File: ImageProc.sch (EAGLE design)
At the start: 93 parts, among them IC1 XC61GC3002HR-G, IC2 MIC5335-SPYMT, IC5 AT86RF233-ZU, IC6 LTC6088, IC7 DRV8833RTY, IC8 DRV8833RTY, IC9 MPU-6000, J1 CON-HRS-DM3AT, P1 BAT+, P10 MD2, P2 BAT-, P3 MA1, P4 MA2, P5 MB1, P6 MB2, P7 MC1, P8 MC2, P9 MD1, U1 CY8C5688LTI-LP086

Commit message: Major board layout jumble. Lots of placeholder connections.
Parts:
- removed R12, R17, R22: 15k, biomimetic:RESISTOR0402-RES
- removed R16, R18: 4.7k, biomimetic:RESISTOR0402-RES
- added JP6: USBSMD, SparkFun-Connectors:USBSMD
- R8: device biomimetic:RESISTOR0402-RES -> OPL Eagle Library:R-4R; TOLERANCE 1% -> (none)
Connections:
- removed net !SS2_2: IC9S.!CS
- new net !SS2: IC9S.!CS, U1G$6./SS2_2
- new net EMFILE_CS: U1G$3.EMFILE_CS
- new net EMFILE_MISO: U1G$3.EMFILE_MISO
- new net EMFILE_MOSI: U1G$3.EMFILE_MOSI
- new net EMFILE_SCK: U1G$3.EMFILE_SCK
- new net USB_D+: JP6.D+, U1G$6.USB_D+
- new net USB_D-: JP6.D-, U1G$6.USB_D-
- net !SS1: now also U1G$6./SS1
- net 3.3V: now also J1.VDD; no longer R16.2
- net BATT_LEVEL: now also U1G$1.VBATT_SENSE
- net GND: now also J1.VSS; no longer R18.1
- net GN_LED: now also U1G$4.GREEN_LED
- net MOTOR_A_BEMF: now also U1G$1.BEMFA
- net MOTOR_A_IN1: now also U1G$5.PWMA_1
- net MOTOR_A_IN2: now also U1G$5.PWMA_2
- net MOTOR_B_BEMF: now also U1G$1.BEMFB
- net MOTOR_B_IN1: now also U1G$5.PWMB_1
- net MOTOR_B_IN2: now also U1G$5.PWMB_2
- net MOTOR_C_BEMF: now also U1G$1.BEMFC
- net MOTOR_C_IN1: now also U1G$5.PWMC_1
- net MOTOR_C_IN2: now also U1G$5.PWMC_2
- net MOTOR_D_BEMF: now also U1G$1.BEMFD
- net MOTOR_D_IN1: now also U1G$5.PWMD_1
- net MOTOR_D_IN2: now also U1G$5.PWMD_2
- net N$22: now also R8B.1; no longer R12.1
- net N$24: now also R8C.1; no longer R17.1
- net N$26: now also R8D.1; no longer R22.1
- net N$30: now also R8A.1; no longer R8.1
- net N$34: now also R8D.2; no longer R22.2
- net N$35: now also R8C.2; no longer R17.2
- net N$36: now also R8A.2; no longer R8.2
- net N$37: now also R8B.2; no longer R12.2
- net RD_LED: now also U1G$4.RED_LED
- net SCK1: now also U1G$6.SCK1
- net SCK2: now also U1G$6.SCK2
- net SCL1: now also U1G$6.SCL1
- net SDA1: now also U1G$6.SDA1
- net SDI1: now also U1G$6.MISO1
- net SDI2: now also U1G$6.MISO2
- net SDO1: now also U1G$6.MOSI1
- net SDO2: now also U1G$6.MOSI2
- net V_REF: no longer R16.1, R18.2
- net YW_LED: now also U1G$4.YELLOW_LED
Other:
- moved on the sheet: C26, R4, R5, U1G$1, U1G$2, U1G$3, U1G$4, U1G$6

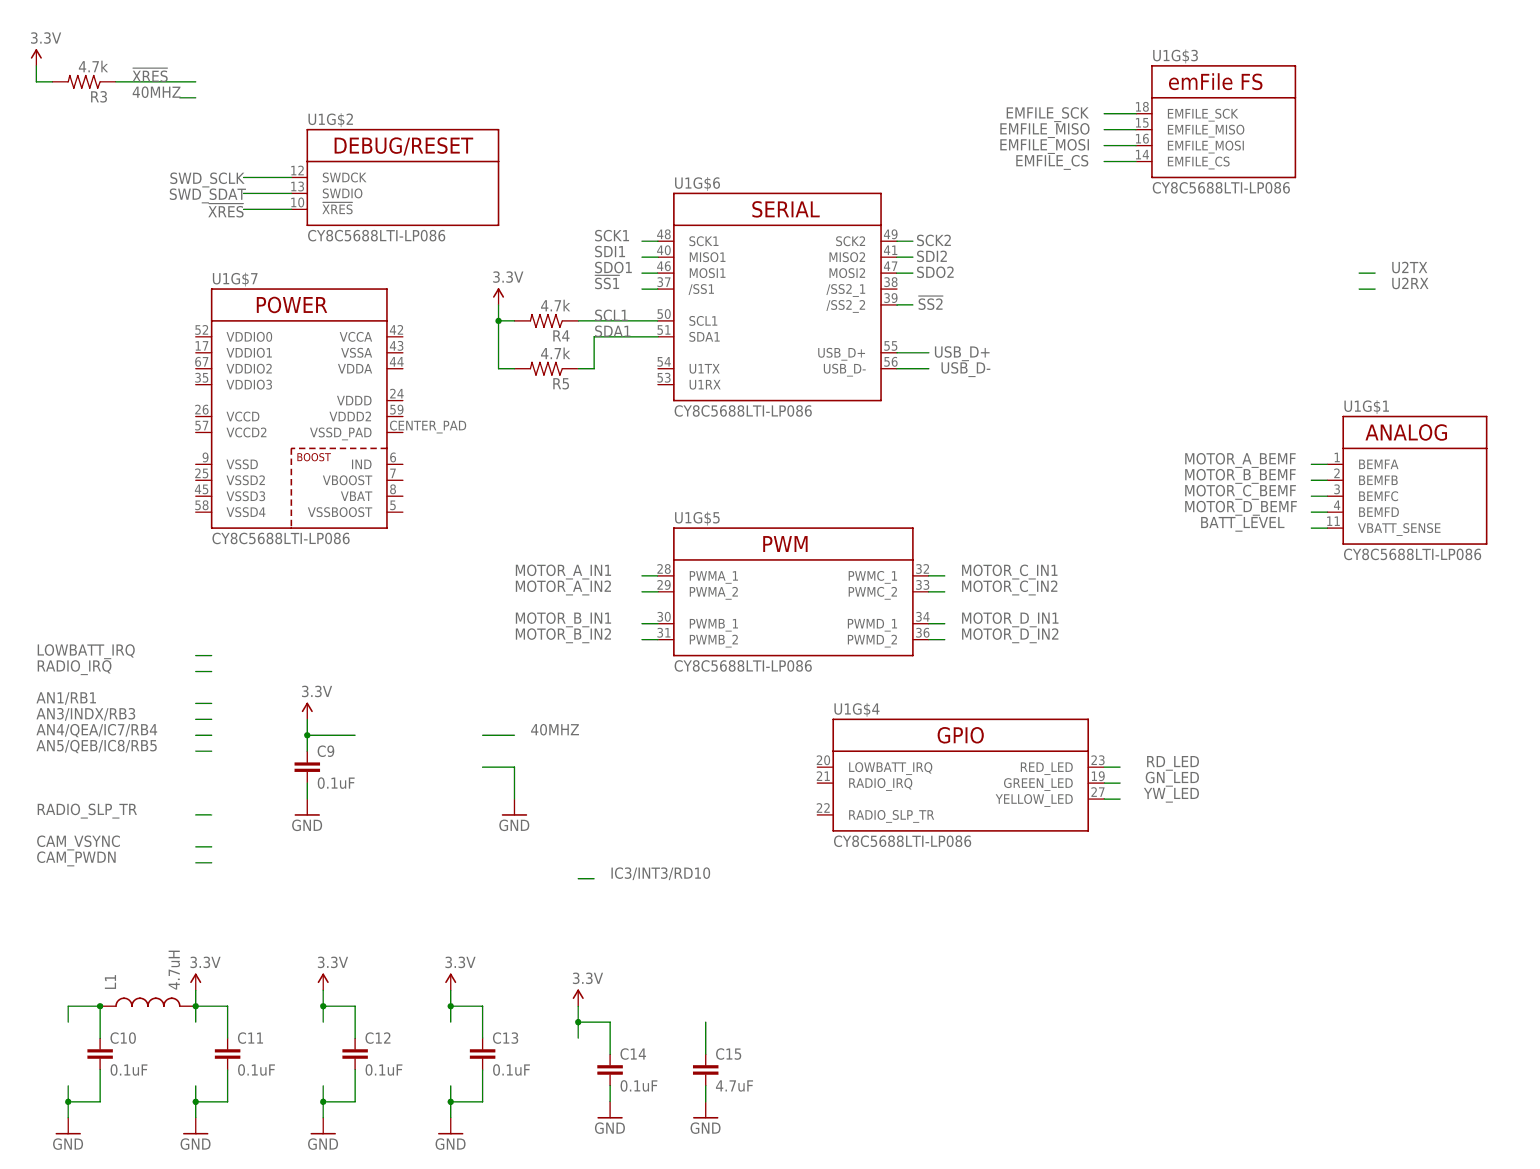
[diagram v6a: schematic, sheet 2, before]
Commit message: Power routing now in schematic. Prelim boost converter components.
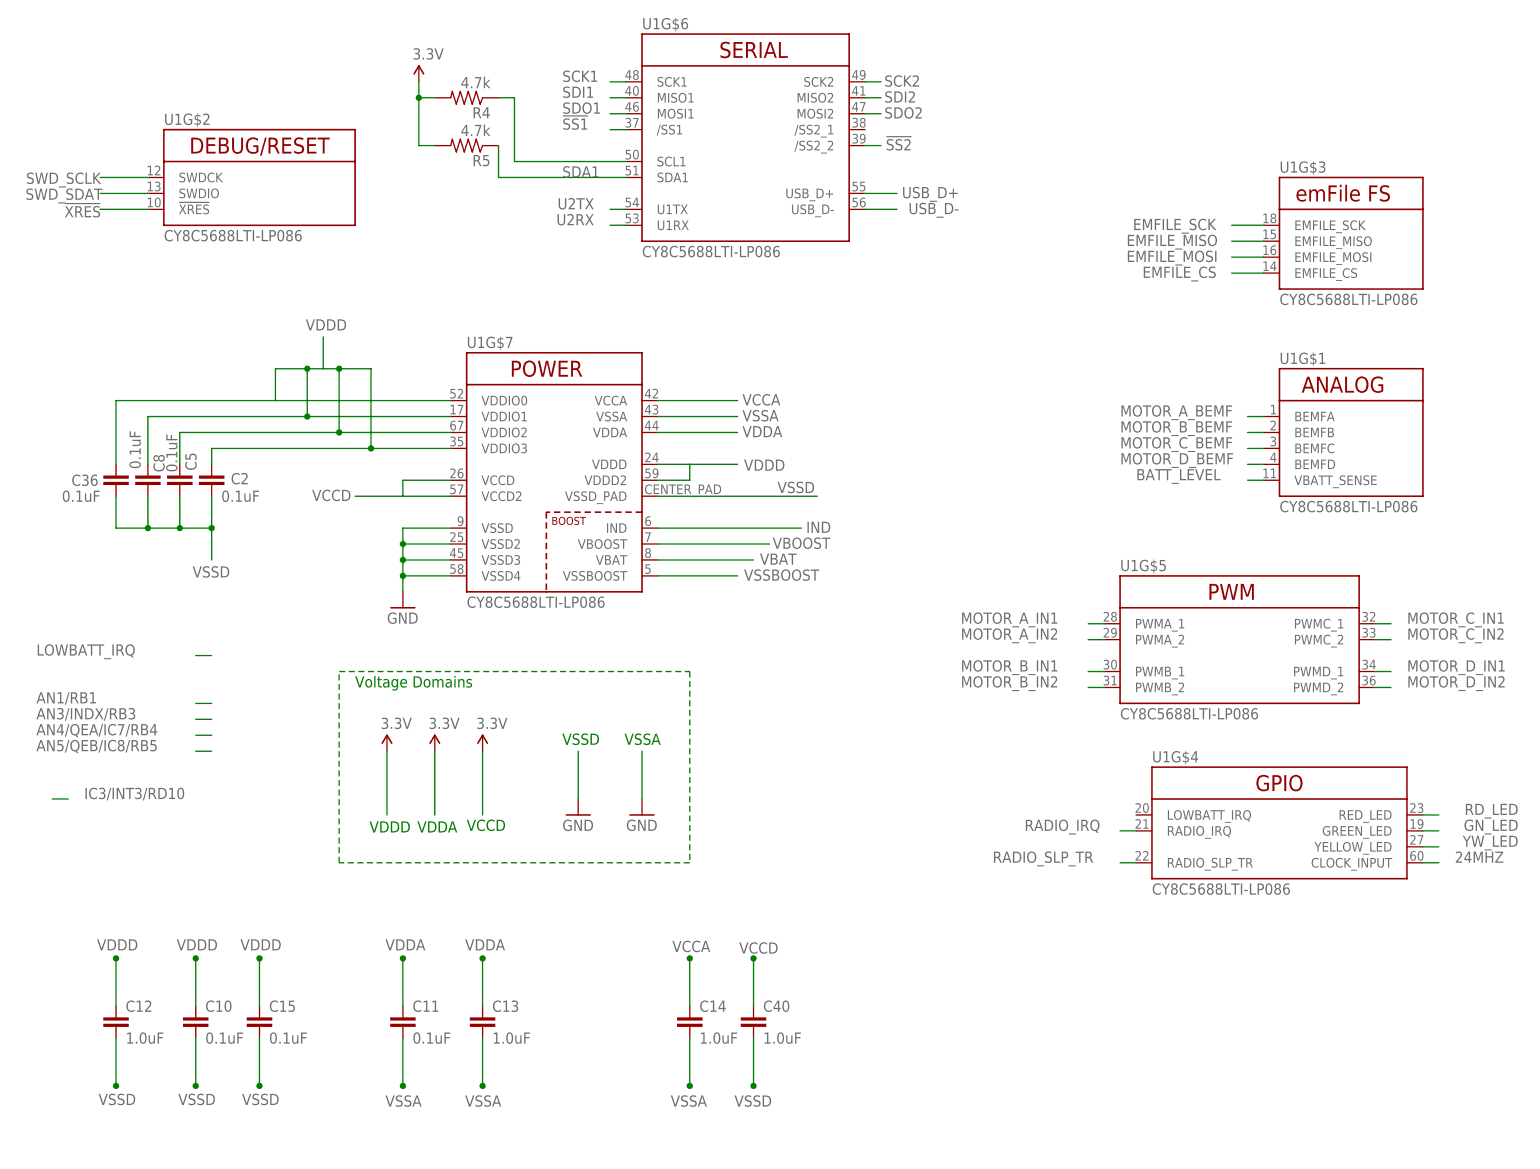
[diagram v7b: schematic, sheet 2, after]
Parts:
- removed R3: 4.7k, biomimetic:RESISTOR0402-RES
- added C2, C36, C5, C8: 0.1uF, biomimetic:CAP0402-CAP
- added C40: 1.0uF, biomimetic:CAP0402-CAP
- added C45: 22uF, biomimetic:CAP0805
- added C46: .1uF, biomimetic:CAP0603-CAP
- added D1: (no value), diode:DIODE-SOD123
- C12, C13, C14: value 0.1uF -> 1.0uF
- C15: value 4.7uF -> 0.1uF; device biomimetic:CAP0603-CAP -> biomimetic:CAP0402-CAP; COMMENT ESR < 5 Ohm -> (none); TECHNOLOGY CERAMIC -> (none); VOLTAGE 16V -> (none)
- C9: value 0.1uF -> 22uF; device biomimetic:CAP0402-CAP -> biomimetic:CAP0805
- L1: value 4.7uH -> 10uH; device biomimetic:INDUCTOR0603 -> pullin:SRN3015-100M
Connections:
- removed net N$28: C15.1
- new net 24MHZ: U1G$4.CLOCK_INPUT
- new net IND: D1.A, L1.2, U1G$7.IND
- new net VBAT: C9.1, L1.1, U1G$7.VBAT
- new net VBOOST: U1G$7.VBOOST
- new net VCCA: C14.1, U1G$7.VCCA
- new net VCCD: C40.1, U1G$7.VCCD, U1G$7.VCCD2
- new net VDDA: C11.1, C13.1, U1G$7.VDDA
- new net VDDD: C10.1, C12.1, C15.1, C2.1, C36.1, C45.1, C46.1, C5.1, C8.1, D1.C, U1G$7.VDDD, U1G$7.VDDD2, U1G$7.VDDIO0, U1G$7.VDDIO1, U1G$7.VDDIO2, U1G$7.VDDIO3
- new net VSSA: C11.2, C13.2, C14.2, C45.2, C46.2, U1G$7.VSSA
- new net VSSBOOST: C9.2, U1G$7.VSSBOOST
- new net VSSD: C10.2, C12.2, C15.2, C2.2, C36.2, C40.2, C5.2, C8.2, U1G$7.VSSD, U1G$7.VSSD2, U1G$7.VSSD3, U1G$7.VSSD4, U1G$7.VSSD_PAD
- net !XRES: now also U1G$2.!XRES; no longer R3.1
- net 3.3V: no longer C11.1, C12.1, C13.1, C14.1, C9.1, L1.2, R3.2
- net GND: no longer C10.2, C11.2, C12.2, C13.2, C14.2, C15.2, C9.2
- net MOTOR_A_OUT1: now also R33A.1
- net MOTOR_A_OUT2: now also R33B.1
- net N$21: now also R4.1, U1G$6.SCL1; no longer C10.1, L1.1
- net RADIO_IRQ: now also U1G$4.RADIO_IRQ
- net RADIO_SLP_TR: now also U1G$4.RADIO_SLP_TR
- net SCL1: no longer R4.1, U1G$6.SCL1
- net SWD_SCLK: now also U1G$2.SWDCK
- net SWD_SDAT: now also U1G$2.SWDIO
- net U2RX: now also U1G$6.U1RX
- net U2TX: now also U1G$6.U1TX
- net V_REF: now also R35A.2
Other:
- note added: "Boost Converter"
- note added: "VCCD"
- note added: "VDDA"
- note added: "VDDD"
- note added: "VSSA"
- note added: "VSSD"
- note added: "Vin for boost"
- note added: "Voltage Domains"
- moved on the sheet: C1, C10, C11, C12, C13, C14, C15, C3, C4, C6, C7, IC1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

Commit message: Proof of concept: signal routing for radio, gyro, and debug port into PSOC arbitrary pins.
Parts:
- removed IC6: LTC6088, biomimetic:LTC6088
- removed LED_RX: GREEN, biomimetic:LED0603
- removed LED_TX: RED, biomimetic:LED0603
- removed R35: 15k, OPL Eagle Library:R-4R
- removed R6, R7: 2.7k, biomimetic:RESISTOR0402-RES
- added C47: 0.1uF, biomimetic:CAP0402-CAP
- added C48, C49: 15pF, biomimetic:CAP0402-CAP
- added IC3, IC4: LTC6087, biomimetic:LTC6087
- added U2: SIT8008AI-72-33E-24.000000G, pullin:SIT8008AI-72-33E-24.000000G
- C46: value .1uF -> 0.1uF; device biomimetic:CAP0603-CAP -> biomimetic:CAP0402-CAP
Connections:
- removed net N$11: LED_RX.C, R7.1
- removed net N$5: LED_TX.C, R6.1
- new net N$33: JP6.VBUS
- net !SS2: now also U1G$6./SS2; no longer U1G$6./SS2_2
- net 24MHZ: now also C48.1
- net 3.3V: now also C47.1, C49.1, IC3P.V+, IC4P.V+, U2.OE/!ST, U2.VDD; no longer IC6P.V+
- net EMFILE_CS: now also J1.CD/DAT3
- net EMFILE_MISO: now also J1.DAT0
- net EMFILE_MOSI: now also J1.CMD
- net EMFILE_SCK: now also J1.CLK
- net GND: now also C47.2, C48.2, C49.2, IC3P.V-, IC4P.V-, JP6.GND, U1G$7.VSSD, U1G$7.VSSD2, U1G$7.VSSD3, U1G$7.VSSD4, U2.GND; no longer IC6P.V-, R6.2, R7.2
- net MOTOR_B_OUT1: now also R33C.1
- net MOTOR_B_OUT2: now also R33D.1
- net MOTOR_C_OUT1: now also R34A.1
- net MOTOR_C_OUT2: now also R34B.1
- net MOTOR_D_OUT1: now also R34C.1
- net MOTOR_D_OUT2: now also R34D.1
- net N$13: no longer LED_RX.A
- net N$14: no longer LED_TX.A
- net N$22: now also IC3B.+IN; no longer IC6B.-IN
- net N$23: now also IC3B.-IN, R8D.2; no longer IC6B.+IN, R35B.1
- net N$24: now also IC4A.+IN; no longer IC6C.-IN, R8C.1
- net N$25: now also IC4A.-IN; no longer IC6C.+IN, R35C.1
- net N$26: now also IC4B.+IN; no longer IC6D.-IN, R8D.1
- net N$27: now also IC4B.-IN; no longer IC6D.+IN, R35D.1
- net N$30: now also IC3A.+IN; no longer IC6A.-IN
- net N$31: now also IC3A.-IN, R8C.2; no longer IC6A.+IN, R35A.1
- net N$34: now also IC4B.OUT; no longer IC6D.OUT, R8D.2
- net N$35: now also IC4A.OUT; no longer IC6C.OUT, R8C.2
- net N$36: now also IC3A.OUT; no longer IC6A.OUT
- net N$37: now also IC3B.OUT; no longer IC6B.OUT
- net VSSD: no longer U1G$7.VSSD, U1G$7.VSSD2, U1G$7.VSSD3, U1G$7.VSSD4
- net V_REF: now also R8C.1, R8D.1; no longer R35A.2
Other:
- moved on the sheet: C29, R8C, R8D, U1G$3
